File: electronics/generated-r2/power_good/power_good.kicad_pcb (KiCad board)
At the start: 2 copper layers, 20 x 20 mm, 6 parts, among them J1 PICO3V3_GND_SENSE3V3_PG, U1 TPS3808G33DBVR

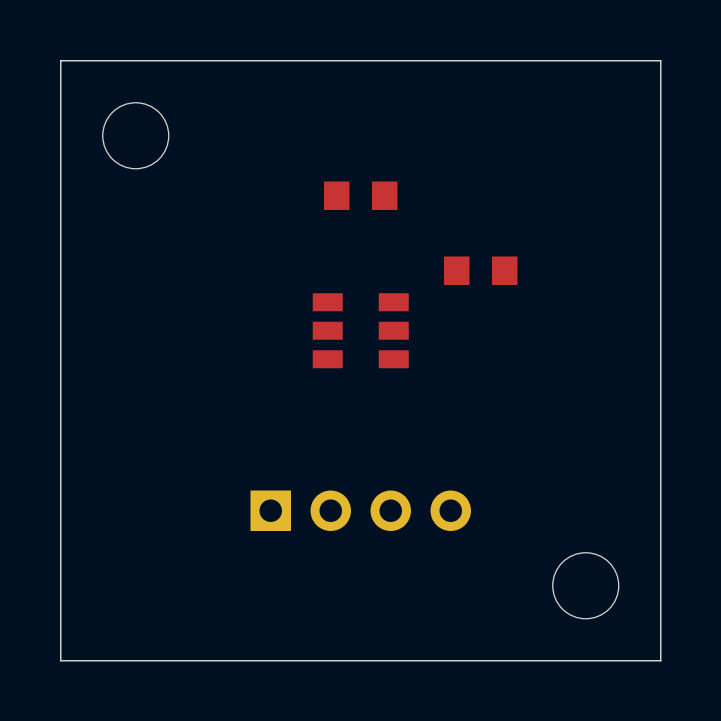
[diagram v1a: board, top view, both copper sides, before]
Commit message: build(r2): publish verified four-board electronics baseline [skip ci]
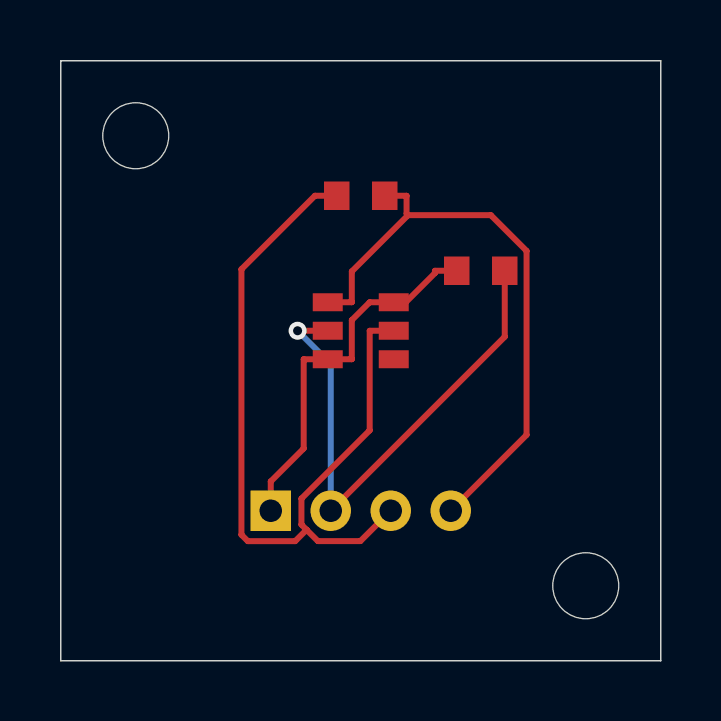
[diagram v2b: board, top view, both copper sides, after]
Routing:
- net SENS_3V3: track 0.00 -> 27.3 mm
- net POWER_GOOD: track 0.00 -> 20.0 mm
- net GND: track 0.00 -> 17.9 mm, vias 0 -> 1
- net PICO_3V3: track 0.00 -> 12.6 mm
